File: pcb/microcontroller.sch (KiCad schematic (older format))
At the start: 7 parts

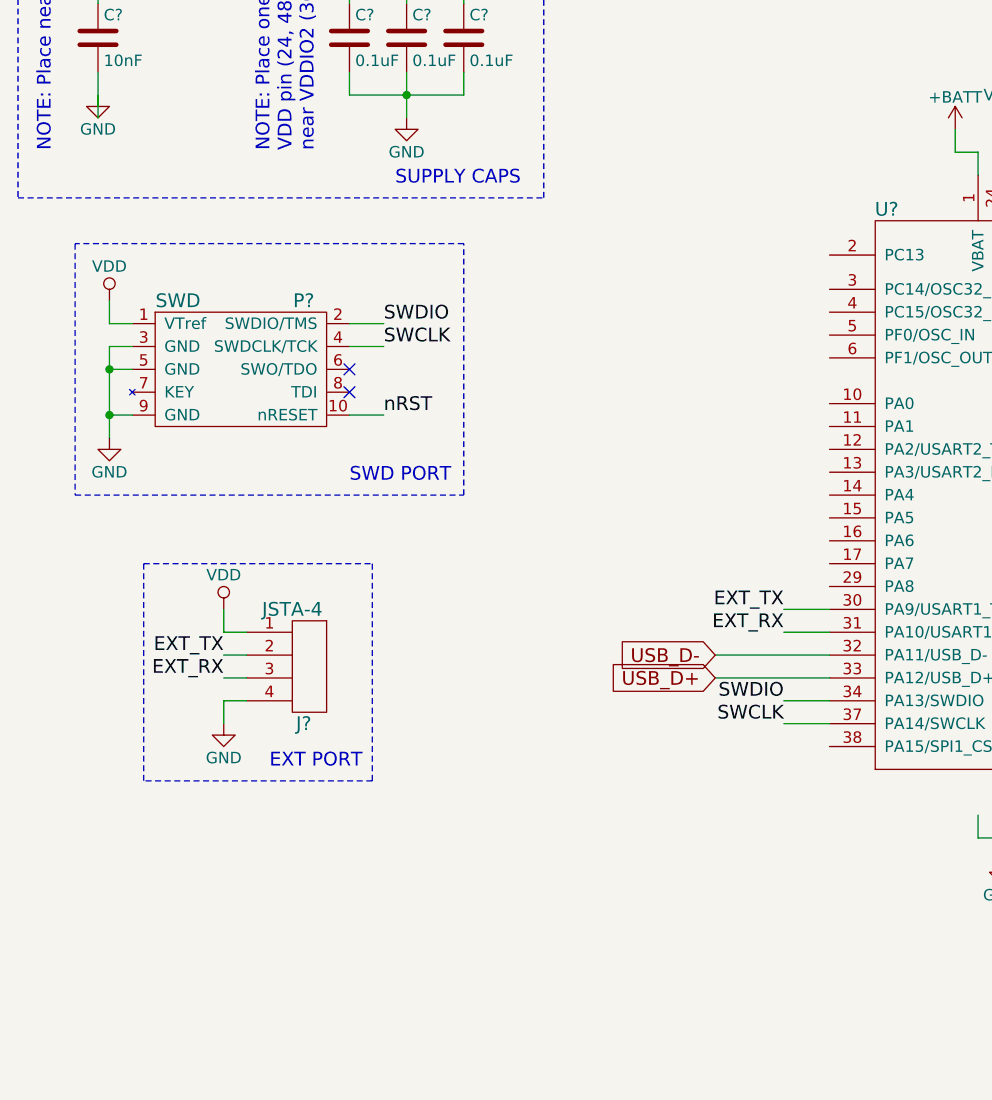
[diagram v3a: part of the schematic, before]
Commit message: Add USB connector to microcontroller sheet
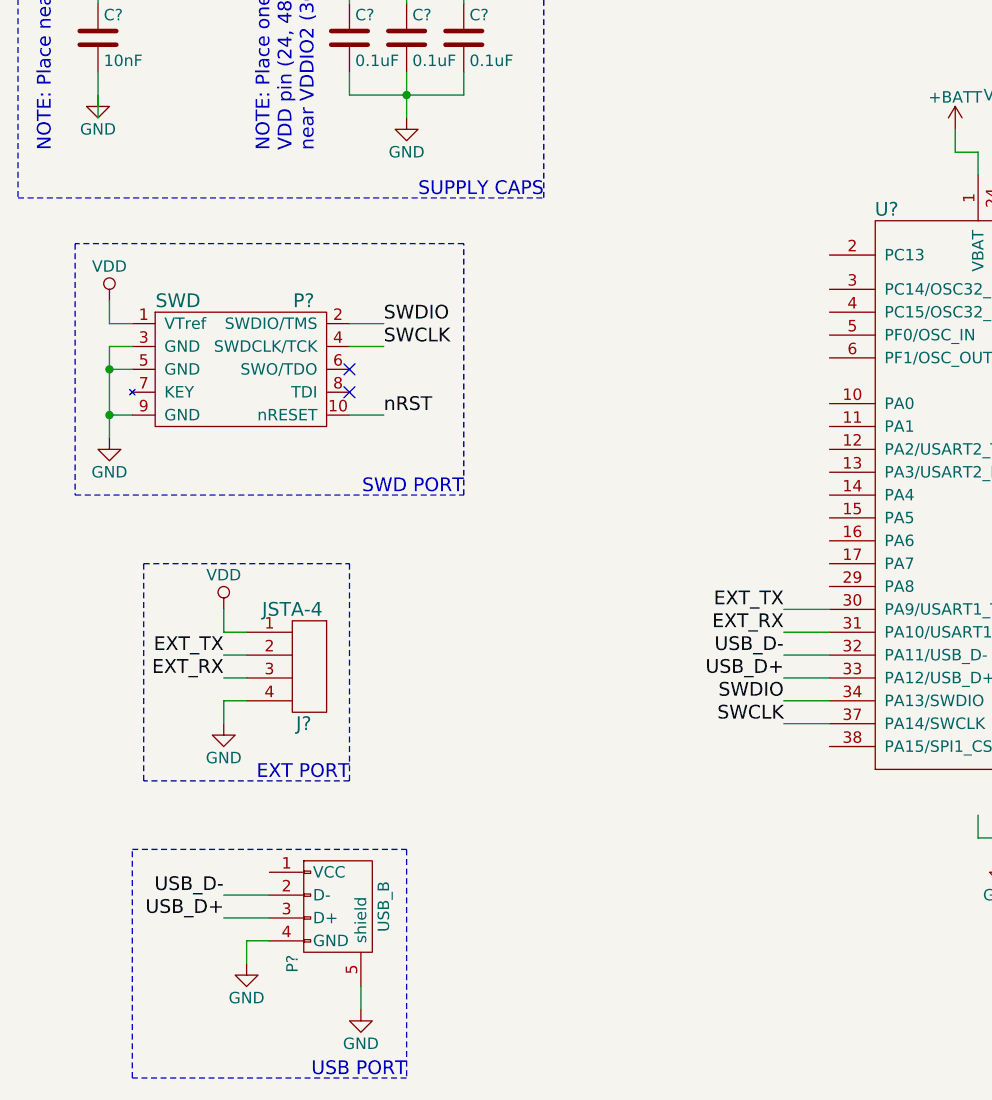
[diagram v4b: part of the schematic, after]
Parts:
- added P?: USB_B, symbol USB_B
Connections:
- wire segments 56 -> 61
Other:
- note added: "USB PORT"
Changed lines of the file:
@@
 	6000 2500 6000 2400
 Wire Wire Line
-	4850 4700 4350 4700
-Wire Wire Line
-	4850 4800 4350 4800
-Text GLabel 4350 4700 0    60   Input ~ 0
-USB_D-
-Text GLabel 4350 4800 0    60   Input ~ 0
-USB_D+
+	4650 4700 4850 4700
+Wire Wire Line
+	4850 4800 4650 4800
 Text Notes 6250 2500 0    60   ~ 0
 NOTE: VDD supply needs 4.7uF across it\nVAA supply needs 1uF across it
@@
 Wire Notes Line
 	3250 2900 1550 2900
-Text Notes 2750 3950 0    60   ~ 0
+Text Notes 3250 4000 2    60   ~ 0
 SWD PORT
 Wire Notes Line
@@
 Wire Notes Line
 	1300 1200 1300 2700
-Text Notes 2950 2650 0    60   ~ 0
+Text Notes 3600 2700 2    60   ~ 0
 SUPPLY CAPS
 Wire Wire Line
@@
 $EndComp
 Wire Notes Line
-	1850 4300 2850 4300
-Wire Notes Line
-	2850 4300 2850 5250
-Wire Notes Line
-	2850 5250 1850 5250
+	1850 4300 2750 4300
+Wire Notes Line
+	2750 4300 2750 5250
+Wire Notes Line
+	2750 5250 1850 5250
 Wire Notes Line
 	1850 5250 1850 4300
-Text Notes 2400 5200 0    60   ~ 0
+Text Notes 2750 5250 2    60   ~ 0
 EXT PORT
+$Comp
+L USB_B P?
+U 1 1 565B7F67
+P 2700 5850
+F 0 "P?" H 2900 5650 50  0000 C CNN
+F 1 "USB_B" H 2650 6050 50  0000 C CNN
+F 2 "" V 2650 5750 60  0000 C CNN
+F 3 "" V 2650 5750 60  0000 C CNN
+	1    2700 5850
+	0    1    1    0
+$EndComp
+$Comp
+L GND #PWR?
+U 1 1 565B80EF
+P 2300 6050
+F 0 "#PWR?" H 2300 5800 50  0001 C CNN
+F 1 "GND" H 2300 5900 50  0000 C CNN
+F 2 "" H 2300 6050 60  0000 C CNN
+F 3 "" H 2300 6050 60  0000 C CNN
+	1    2300 6050
+	1    0    0    -1
+$EndComp
+$Comp
+L GND #PWR?
+U 1 1 565B8112
+P 2800 6250
+F 0 "#PWR?" H 2800 6000 50  0001 C CNN
+F 1 "GND" H 2800 6100 50  0000 C CNN
+F 2 "" H 2800 6250 60  0000 C CNN
+F 3 "" H 2800 6250 60  0000 C CNN
+	1    2800 6250
+	1    0    0    -1
+$EndComp
+Wire Wire Line
+	2800 6150 2800 6250
+Wire Wire Line
+	2400 5950 2300 5950
+Wire Wire Line
+	2300 5950 2300 6050
+Wire Wire Line
+	2400 5850 2200 5850
+Wire Wire Line
+	2400 5750 2200 5750
+Text Label 4650 4700 2    60   ~ 0
+USB_D-
+Text Label 4650 4800 2    60   ~ 0
+USB_D+
+Text Label 2200 5750 2    60   ~ 0
+USB_D-
+Text Label 2200 5850 2    60   ~ 0
+USB_D+
+Wire Notes Line
+	1800 5550 3000 5550
+Wire Notes Line
+	3000 5550 3000 6550
+Wire Notes Line
+	3000 6550 1800 6550
+Wire Notes Line
+	1800 6550 1800 5550
+Text Notes 3000 6550 2    60   ~ 0
+USB PORT
 $EndSCHEMATC

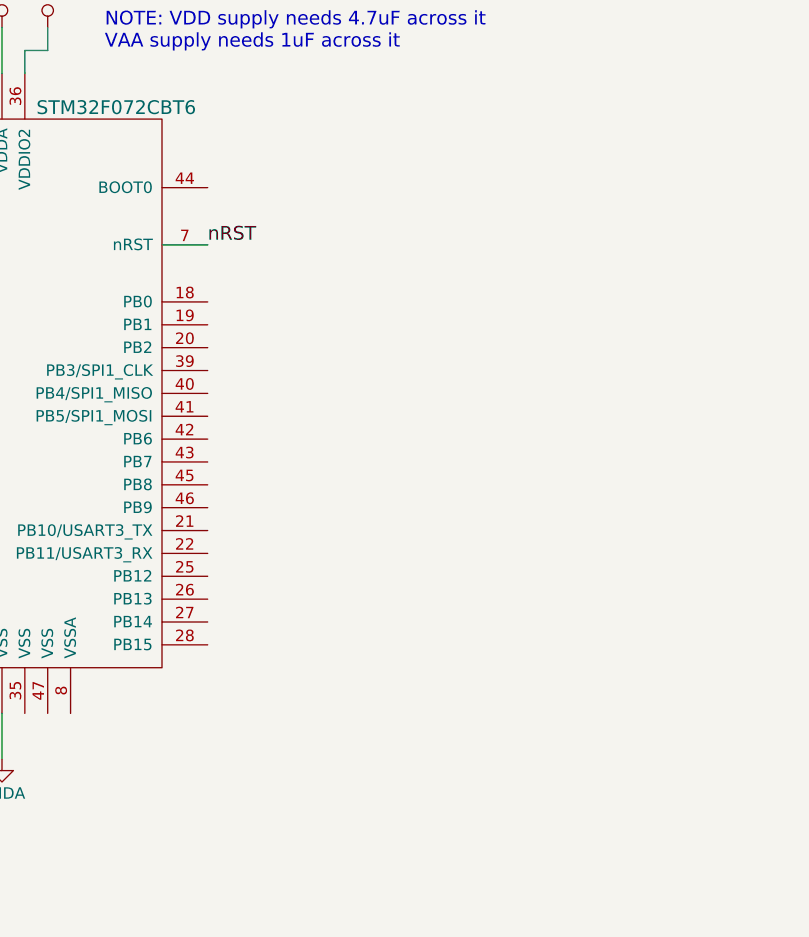
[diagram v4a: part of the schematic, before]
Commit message: Add bootloader select switch to microcontroller sheet
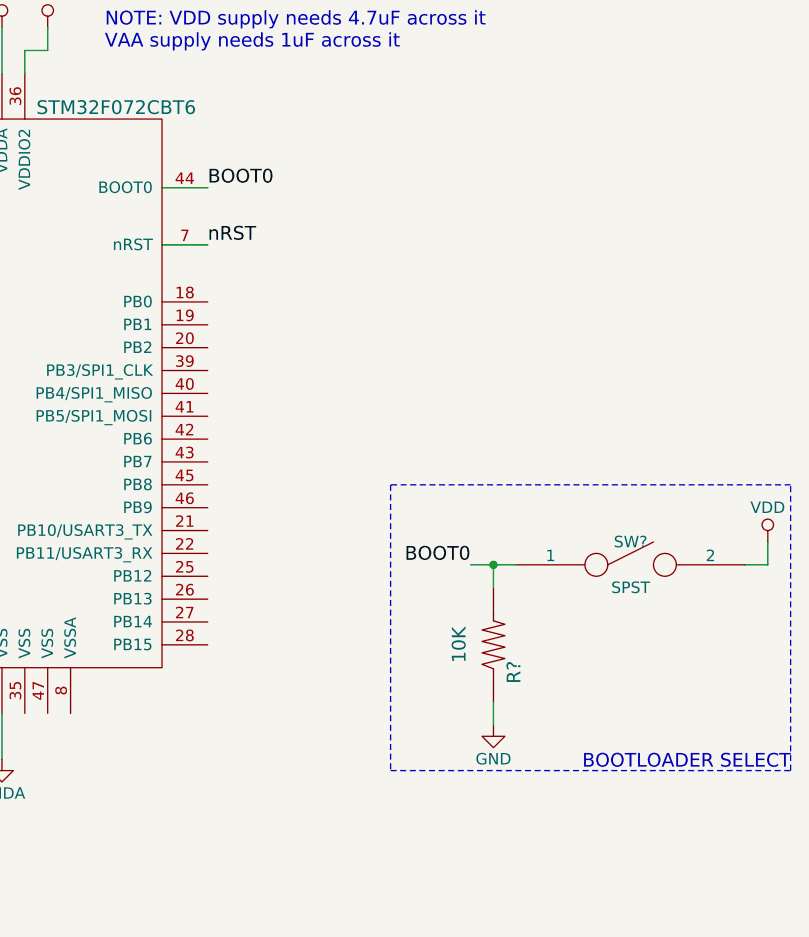
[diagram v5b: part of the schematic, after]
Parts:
- added R?: 10K, symbol RESISTOR
- added SW?: SPST, symbol SPST
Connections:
- net labels added: BOOT0
- wire segments 61 -> 68
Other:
- note added: "BOOTLOADER SELECT"
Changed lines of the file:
@@
 Text Notes 3000 6550 2    60   ~ 0
 USB PORT
+Wire Wire Line
+	6500 3100 6700 3100
+Text Label 6700 3100 0    60   ~ 0
+BOOT0
+$Comp
+L SPST SW?
+U 1 1 565B9D59
+P 8550 4750
+F 0 "SW?" H 8550 4850 50  0000 C CNN
+F 1 "SPST" H 8550 4650 50  0000 C CNN
+F 2 "" H 8550 4750 60  0000 C CNN
+F 3 "" H 8550 4750 60  0000 C CNN
+	1    8550 4750
+	1    0    0    -1
+$EndComp
+Wire Wire Line
+	8050 4750 7950 4750
+Wire Wire Line
+	7950 4750 7850 4750
+Text Label 7850 4750 2    60   ~ 0
+BOOT0
+$Comp
+L VDD #PWR?
+U 1 1 565BA33C
+P 9150 4650
+F 0 "#PWR?" H 9150 4500 50  0001 C CNN
+F 1 "VDD" H 9150 4800 50  0000 C CNN
+F 2 "" H 9150 4650 60  0000 C CNN
+F 3 "" H 9150 4650 60  0000 C CNN
+	1    9150 4650
+	1    0    0    -1
+$EndComp
+Wire Wire Line
+	9050 4750 9150 4750
+Wire Wire Line
+	9150 4750 9150 4650
+$Comp
+L RESISTOR R?
+U 1 1 565BA71B
+P 7950 5100
+F 0 "R?" H 8070 5190 60  0000 C CNN
+F 1 "10K" H 7950 4950 60  0000 C CNN
+F 2 "" H 7950 5100 60  0000 C CNN
+F 3 "" H 7950 5100 60  0000 C CNN
+	1    7950 5100
+	0    1    1    0
+$EndComp
+$Comp
+L GND #PWR?
+U 1 1 565BAC22
+P 7950 5450
+F 0 "#PWR?" H 7950 5200 50  0001 C CNN
+F 1 "GND" H 7950 5300 50  0000 C CNN
+F 2 "" H 7950 5450 60  0000 C CNN
+F 3 "" H 7950 5450 60  0000 C CNN
+	1    7950 5450
+	1    0    0    -1
+$EndComp
+Wire Wire Line
+	7950 5450 7950 5350
+Wire Wire Line
+	7950 4850 7950 4750
+Connection ~ 7950 4750
+Wire Notes Line
+	9250 4400 7500 4400
+Wire Notes Line
+	7500 4400 7500 5650
+Wire Notes Line
+	7500 5650 9250 5650
+Wire Notes Line
+	9250 5650 9250 4400
+Text Notes 9250 5650 2    60   ~ 0
+BOOTLOADER SELECT
 $EndSCHEMATC

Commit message: Add MTX2 circuit and add a sheet for power supply/regulation
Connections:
- wire segments 68 -> 58
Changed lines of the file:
@@
 LIBS:max-7q
 LIBS:ms5611-01ba03
-LIBS:quarter_wave_ant
 LIBS:resistor
 LIBS:rfm69w
-LIBS:sma
 LIBS:stm32f405vgt
 LIBS:swd
@@
 LIBS:stm32f072cbt6
 LIBS:jsta
+LIBS:sma
+LIBS:cga0402mlc-12g
 LIBS:woodchuck-cache
 EELAYER 25 0
@@
 $Descr A4 11693 8268
 encoding utf-8
-Sheet 4 6
+Sheet 4 7
 Title ""
 Date ""
@@
 $EndComp
 $Comp
-L GND #PWR01
+L GND #PWR03
 U 1 1 565B23CF
 P 5600 5600
-F 0 "#PWR01" H 5600 5350 50  0001 C CNN
+F 0 "#PWR03" H 5600 5350 50  0001 C CNN
 F 1 "GND" H 5600 5450 50  0000 C CNN
 F 2 "" H 5600 5600 60  0000 C CNN
@@
 $EndComp
 $Comp
-L GNDA #PWR02
+L GNDA #PWR04
 U 1 1 565B2430
 P 5800 5600
-F 0 "#PWR02" H 5800 5350 50  0001 C CNN
+F 0 "#PWR04" H 5800 5350 50  0001 C CNN
 F 1 "GNDA" H 5800 5450 50  0000 C CNN
 F 2 "" H 5800 5600 60  0000 C CNN
@@
 	5500 5400 5500 5500
 Wire Wire Line
-	5500 5500 5600 5500
-Wire Wire Line
-	5600 5500 5700 5500
-Wire Wire Line
-	5600 5400 5600 5500
-Wire Wire Line
-	5600 5500 5600 5600
+	5500 5500 5700 5500
+Wire Wire Line
+	5600 5400 5600 5600
 Connection ~ 5600 5500
 Wire Wire Line
@@
 $EndComp
 $Comp
-L VDD #PWR03
+L VDD #PWR05
 U 1 1 565B24B5
 P 5600 2400
-F 0 "#PWR03" H 5600 2250 50  0001 C CNN
+F 0 "#PWR05" H 5600 2250 50  0001 C CNN
 F 1 "VDD" H 5600 2550 50  0000 C CNN
 F 2 "" H 5600 2400 60  0000 C CNN
@@
 $EndComp
 $Comp
-L VAA #PWR04
+L VAA #PWR06
 U 1 1 565B24CD
 P 5800 2400
-F 0 "#PWR04" H 5800 2250 50  0001 C CNN
+F 0 "#PWR06" H 5800 2250 50  0001 C CNN
 F 1 "VAA" H 5800 2550 50  0000 C CNN
 F 2 "" H 5800 2400 60  0000 C CNN
@@
 $EndComp
 $Comp
-L VDD #PWR05
+L VDD #PWR07
 U 1 1 565B24E5
 P 6000 2400
-F 0 "#PWR05" H 6000 2250 50  0001 C CNN
+F 0 "#PWR07" H 6000 2250 50  0001 C CNN
 F 1 "VDD" H 6000 2550 50  0000 C CNN
 F 2 "" H 6000 2400 60  0000 C CNN
@@
 	5700 2500 5600 2500
 Wire Wire Line
-	5600 2400 5600 2500
-Wire Wire Line
-	5600 2500 5600 2600
+	5600 2400 5600 2600
 Connection ~ 5600 2500
 $Comp
-L +BATT #PWR06
+L +BATT #PWR08
 U 1 1 565B2BDD
 P 5400 2400
-F 0 "#PWR06" H 5400 2250 50  0001 C CNN
+F 0 "#PWR08" H 5400 2250 50  0001 C CNN
 F 1 "+BATT" H 5400 2540 50  0000 C CNN
 F 2 "" H 5400 2400 60  0000 C CNN
@@
 	5400 2500 5400 2400
 $Comp
-L VDD #PWR07
+L VDD #PWR09
 U 1 1 565B2C77
 P 3000 1650
-F 0 "#PWR07" H 3000 1500 50  0001 C CNN
+F 0 "#PWR09" H 3000 1500 50  0001 C CNN
 F 1 "VDD" H 3000 1800 50  0000 C CNN
 F 2 "" H 3000 1650 60  0000 C CNN
@@
 $EndComp
 Wire Wire Line
-	3000 1650 3000 1750
-Wire Wire Line
-	3000 1750 3000 1850
-$Comp
-L GND #PWR08
+	3000 1650 3000 1850
+$Comp
+L GND #PWR010
 U 1 1 565B2D06
 P 3000 2350
-F 0 "#PWR08" H 3000 2100 50  0001 C CNN
+F 0 "#PWR010" H 3000 2100 50  0001 C CNN
 F 1 "GND" H 3000 2200 50  0000 C CNN
 F 2 "" H 3000 2350 60  0000 C CNN
@@
 $EndComp
 Wire Wire Line
-	3000 2150 3000 2250
-Wire Wire Line
-	3000 2250 3000 2350
+	3000 2150 3000 2350
 $Comp
 L C C?
@@
 NOTE: Place one near each\nVDD pin (24, 48) and one\nnear VDDIO2 (36)
 Wire Wire Line
-	2750 2250 3000 2250
-Wire Wire Line
-	3000 2250 3250 2250
-Wire Wire Line
-	2750 1750 3000 1750
-Wire Wire Line
-	3000 1750 3250 1750
+	2750 2250 3250 2250
+Wire Wire Line
+	2750 1750 3250 1750
 $Comp
 L C C?
@@
 $EndComp
 $Comp
-L VDD #PWR09
+L VDD #PWR011
 U 1 1 565B33A3
 P 1650 1750
-F 0 "#PWR09" H 1650 1600 50  0001 C CNN
+F 0 "#PWR011" H 1650 1600 50  0001 C CNN
 F 1 "VDD" H 1650 1900 50  0000 C CNN
 F 2 "" H 1650 1750 60  0000 C CNN
@@
 	1650 1750 1650 1850
 $Comp
-L GND #PWR010
+L GND #PWR012
 U 1 1 565B33AB
 P 1650 2250
-F 0 "#PWR010" H 1650 2000 50  0001 C CNN
+F 0 "#PWR012" H 1650 2000 50  0001 C CNN
 F 1 "GND" H 1650 2100 50  0000 C CNN
 F 2 "" H 1650 2250 60  0000 C CNN
@@
 SWCLK
 $Comp
-L VDD #PWR?
+L VDD #PWR013
 U 1 1 565B450F
 P 1700 3150
-F 0 "#PWR?" H 1700 3000 50  0001 C CNN
+F 0 "#PWR013" H 1700 3000 50  0001 C CNN
 F 1 "VDD" H 1700 3300 50  0000 C CNN
 F 2 "" H 1700 3150 60  0000 C CNN
@@
 	1700 3250 1700 3150
 $Comp
-L GND #PWR?
+L GND #PWR014
 U 1 1 565B4620
 P 1700 3750
-F 0 "#PWR?" H 1700 3500 50  0001 C CNN
+F 0 "#PWR014" H 1700 3500 50  0001 C CNN
 F 1 "GND" H 1700 3600 50  0000 C CNN
 F 2 "" H 1700 3750 60  0000 C CNN
@@
 	1700 3650 1800 3650
 Wire Wire Line
-	1700 3350 1700 3450
-Wire Wire Line
-	1700 3450 1700 3650
-Wire Wire Line
-	1700 3650 1700 3750
+	1700 3350 1700 3750
 Wire Wire Line
 	1800 3450 1700 3450
@@
 EXT_RX
 $Comp
-L GND #PWR?
+L GND #PWR015
 U 1 1 565B6C28
 P 2200 5000
-F 0 "#PWR?" H 2200 4750 50  0001 C CNN
+F 0 "#PWR015" H 2200 4750 50  0001 C CNN
 F 1 "GND" H 2200 4850 50  0000 C CNN
 F 2 "" H 2200 5000 60  0000 C CNN
@@
 $EndComp
 $Comp
-L VDD #PWR?
+L VDD #PWR016
 U 1 1 565B6CE2
 P 2200 4500
-F 0 "#PWR?" H 2200 4350 50  0001 C CNN
+F 0 "#PWR016" H 2200 4350 50  0001 C CNN
 F 1 "VDD" H 2200 4650 50  0000 C CNN
 F 2 "" H 2200 4500 60  0000 C CNN
@@
 $EndComp
 $Comp
-L GND #PWR?
+L GND #PWR017
 U 1 1 565B80EF
 P 2300 6050
-F 0 "#PWR?" H 2300 5800 50  0001 C CNN
+F 0 "#PWR017" H 2300 5800 50  0001 C CNN
 F 1 "GND" H 2300 5900 50  0000 C CNN
 F 2 "" H 2300 6050 60  0000 C CNN
@@
 $EndComp
 $Comp
-L GND #PWR?
+L GND #PWR018
 U 1 1 565B8112
 P 2800 6250
-F 0 "#PWR?" H 2800 6000 50  0001 C CNN
+F 0 "#PWR018" H 2800 6000 50  0001 C CNN
 F 1 "GND" H 2800 6100 50  0000 C CNN
 F 2 "" H 2800 6250 60  0000 C CNN
@@
 $EndComp
 Wire Wire Line
-	8050 4750 7950 4750
-Wire Wire Line
-	7950 4750 7850 4750
+	7850 4750 8050 4750
 Text Label 7850 4750 2    60   ~ 0
 BOOT0
 $Comp
-L VDD #PWR?
+L VDD #PWR019
 U 1 1 565BA33C
 P 9150 4650
-F 0 "#PWR?" H 9150 4500 50  0001 C CNN
+F 0 "#PWR019" H 9150 4500 50  0001 C CNN
 F 1 "VDD" H 9150 4800 50  0000 C CNN
 F 2 "" H 9150 4650 60  0000 C CNN
@@
 $EndComp
 $Comp
-L GND #PWR?
+L GND #PWR020
 U 1 1 565BAC22
 P 7950 5450
-F 0 "#PWR?" H 7950 5200 50  0001 C CNN
+F 0 "#PWR020" H 7950 5200 50  0001 C CNN
 F 1 "GND" H 7950 5300 50  0000 C CNN
 F 2 "" H 7950 5450 60  0000 C CNN
